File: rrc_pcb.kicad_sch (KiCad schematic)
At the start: 15 parts, among them J1 Conn_01x02_Male-Connector, J2 Conn_01x03_Male-Connector, J3 digital logic connection, U1 iridium9602, U2 Teensy4.1, U3 BN220-GPS, U4 ICM-20948, U5 MS5611, U6 logo, U7 voltReg

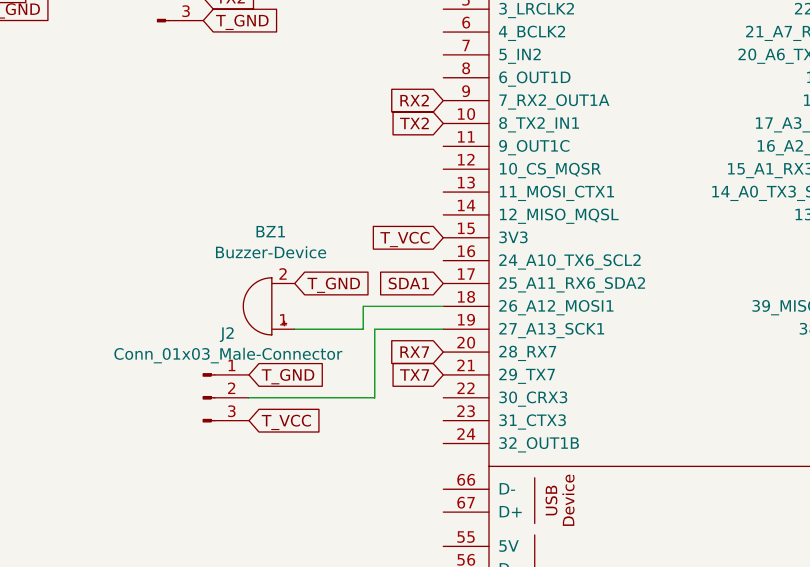
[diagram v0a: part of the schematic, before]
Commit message: fixed rfd traces
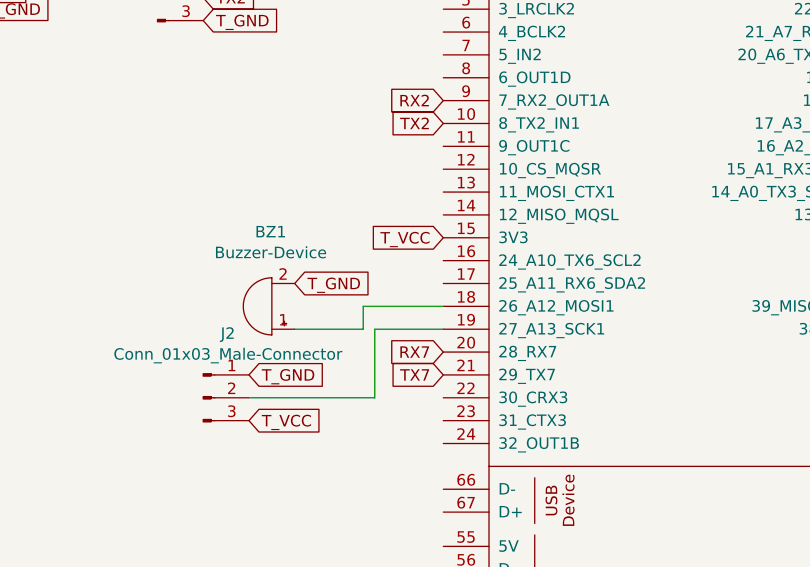
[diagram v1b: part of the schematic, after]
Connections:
- net SDA1: no longer U2.17 (25_A11_RX6_SDA2)
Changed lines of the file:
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@@
-    )
-  )
-  (global_label "SDA1" (shape input) (at 99.06 62.23 180) (fields_autoplaced)
-    (effects (font (size 1.27 1.27)) (justify right))
-    (property "Intersheet References" "${INTERSHEET_REFS}" (id 0) (at 91.9582 62.3094 0)
-      (effects (font (size 1.27 1.27)) (justify right) hide)
     )
   )

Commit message: rfd iteration f3
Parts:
- removed U1: iridium9602, iridium9602:iridium9602, symbol parts:iridium9602
- added RF1: RFD900+-RF_Module, rfd900+:RFD900+, symbol parts:RFD900+-RF_Module
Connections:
- net GND: now also RF1.2 (GND)
- net RX2: now also RF1.9 (SITX)
- net TX2: now also RF1.7 (SIRX)
- net VCC: now also RF1.5 (+5VUSB)
- new net: RF1.4 (+5V), RF1.6 (+5VUSB)
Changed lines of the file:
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@@
 (kicad_sch (version 20211123) (generator eeschema)
   (paper "A4")
+  (wire (pts (xy 36.83 35.56) (xy 36.83 38.1))
+    (stroke (width 0) (type default) (color 0 0 0 0))
+  )
   (wire (pts (xy 241.3 105.41) (xy 229.87 105.41))
     (stroke (width 0) (type default) (color 0 0 0 0))
@@
     )
   )
-  (global_label "TX2" (shape input) (at 47.0887 29.7566 0) (fields_autoplaced)
-    (effects (font (size 1.27 1.27)) (justify left))
-    (property "Intersheet References" "${INTERSHEET_REFS}" (id 0) (at 52.7996 29.6772 0)
-      (effects (font (size 1.27 1.27)) (justify left) hide)
+  (global_label "TX2" (shape input) (at 7.62 40.64 180) (fields_autoplaced)
+    (effects (font (size 1.27 1.27)) (justify right))
+    (property "Intersheet References" "${INTERSHEET_REFS}" (id 0) (at 1.9091 40.7194 0)
+      (effects (font (size 1.27 1.27)) (justify right) hide)
     )
   )
@@
     )
   )
-  (global_label "VCC" (shape input) (at 46.99 15.24 0) (fields_autoplaced)
-    (effects (font (size 1.27 1.27)) (justify left))
-    (property "Intersheet References" "${INTERSHEET_REFS}" (id 0) (at -121.92 -113.03 0)
+  (global_label "VCC" (shape input) (at 7.62 38.1 180) (fields_autoplaced)
+    (effects (font (size 1.27 1.27)) (justify right))
+    (property "Intersheet References" "${INTERSHEET_REFS}" (id 0) (at 176.53 166.37 0)
       (effects (font (size 1.27 1.27)) hide)
     )
@@
     )
   )
-  (global_label "RX2" (shape input) (at 46.99 27.94 0) (fields_autoplaced)
-    (effects (font (size 1.27 1.27)) (justify left))
-    (property "Intersheet References" "${INTERSHEET_REFS}" (id 0) (at 53.0032 27.8606 0)
-      (effects (font (size 1.27 1.27)) (justify left) hide)
+  (global_label "RX2" (shape input) (at 7.62 43.18 180) (fields_autoplaced)
+    (effects (font (size 1.27 1.27)) (justify right))
+    (property "Intersheet References" "${INTERSHEET_REFS}" (id 0) (at 1.6068 43.2594 0)
+      (effects (font (size 1.27 1.27)) (justify right) hide)
     )
   )
@@
     )
   )
-  (global_label "T_GND" (shape input) (at 46.99 31.75 0) (fields_autoplaced)
-    (effects (font (size 1.27 1.27)) (justify left))
-    (property "Intersheet References" "${INTERSHEET_REFS}" (id 0) (at -19.05 -13.97 0)
-      (effects (font (size 1.27 1.27)) hide)
-    )
-  )
   (global_label "T_GND" (shape input) (at 38.1 95.25 0) (fields_autoplaced)
     (effects (font (size 1.27 1.27)) (justify left))
@@
     )
   )
-  (global_label "GND" (shape input) (at 46.99 20.32 0) (fields_autoplaced)
-    (effects (font (size 1.27 1.27)) (justify left))
-    (property "Intersheet References" "${INTERSHEET_REFS}" (id 0) (at -25.4 -81.28 0)
+  (global_label "GND" (shape input) (at 36.83 33.02 0) (fields_autoplaced)
+    (effects (font (size 1.27 1.27)) (justify left))
+    (property "Intersheet References" "${INTERSHEET_REFS}" (id 0) (at -35.56 -68.58 0)
       (effects (font (size 1.27 1.27)) hide)
     )
@@
     (pin "9")
   )
-  (symbol (lib_id "parts:iridium9602") (at 34.29 21.59 0) (unit 1)
+  (symbol (lib_id "rrc_pcb-rescue:Conn_01x03_Male-Connector") (at 67.31 30.48 0) (unit 1)
+    (in_bom yes) (on_board yes)
+    (property "Reference" "J3" (id 0) (at 70.0532 23.3426 0))
+    (property "Value" "digital logic connection" (id 1) (at 72.39 17.78 0))
+    (property "Footprint" "Connector_PinHeader_2.54mm:PinHeader_1x03_P2.54mm_Vertical" (id 2) (at 67.31 30.48 0)
+      (effects (font (size 1.27 1.27)) hide)
+    )
+    (property "Datasheet" "~" (id 3) (at 67.31 30.48 0)
+      (effects (font (size 1.27 1.27)) hide)
+    )
+    (pin "1")
+    (pin "2")
+    (pin "3")
+  )
+  (symbol (lib_id "parts:RFD900+-RF_Module") (at 13.97 33.02 0) (unit 1)
     (in_bom yes) (on_board yes) (fields_autoplaced)
-    (property "Reference" "U1" (id 0) (at 54.61 24.7649 0)
-      (effects (font (size 1.27 1.27)) (justify left))
-    )
-    (property "Value" "iridium9602" (id 1) (at 54.61 27.3049 0)
-      (effects (font (size 1.27 1.27)) (justify left))
-    )
-    (property "Footprint" "iridium9602:iridium9602" (id 2) (at 34.29 21.59 0)
-      (effects (font (size 1.27 1.27)) hide)
-    )
-    (property "Datasheet" "" (id 3) (at 34.29 21.59 0)
+    (property "Reference" "RF1" (id 0) (at 22.225 26.67 0))
+    (property "Value" "RFD900+-RF_Module" (id 1) (at 22.225 29.21 0))
+    (property "Footprint" "rfd900+:RFD900+" (id 2) (at 13.97 33.02 0)
+      (effects (font (size 1.27 1.27)) hide)
+    )
+    (property "Datasheet" "" (id 3) (at 13.97 33.02 0)
       (effects (font (size 1.27 1.27)) hide)
     )
@@
     (pin "15")
     (pin "16")
-    (pin "17")
-    (pin "18")
-    (pin "19")
-    (pin "2")
-    (pin "20")
+    (pin "2")
     (pin "3")
     (pin "4")
@@
     (pin "8")
     (pin "9")
-  )
-  (symbol (lib_id "rrc_pcb-rescue:Conn_01x03_Male-Connector") (at 67.31 30.48 0) (unit 1)
-    (in_bom yes) (on_board yes)
-    (property "Reference" "J3" (id 0) (at 70.0532 23.3426 0))
-    (property "Value" "digital logic connection" (id 1) (at 72.39 17.78 0))
-    (property "Footprint" "Connector_PinHeader_2.54mm:PinHeader_1x03_P2.54mm_Vertical" (id 2) (at 67.31 30.48 0)
-      (effects (font (size 1.27 1.27)) hide)
-    )
-    (property "Datasheet" "~" (id 3) (at 67.31 30.48 0)
-      (effects (font (size 1.27 1.27)) hide)
-    )
-    (pin "1")
-    (pin "2")
-    (pin "3")
   )
   (symbol (lib_id "teensy:Teensy4.1") (at 127 76.2 0) (unit 1)
@@
       (reference "R4") (unit 1) (value "R-Device") (footprint "Resistor_THT:R_Axial_DIN0207_L6.3mm_D2.5mm_P10.16mm_Horizontal")
     )
-    (path "/84f80ca1-29d4-4e34-8c20-e0b5bcec9cb7"
-      (reference "U1") (unit 1) (value "iridium9602") (footprint "iridium9602:iridium9602")
+    (path "/cca84f39-62d3-48b7-ab11-081e484cf270"
+      (reference "RF1") (unit 1) (value "RFD900+-RF_Module") (footprint "rfd900+:RFD900+")
     )
     (path "/e2a4979b-162a-4acf-966e-29cd5e9f5e0d"
